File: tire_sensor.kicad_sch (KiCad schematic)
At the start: 30 parts, among them J1 Conn_02x05_Odd_Even, J2 U.FL, U2 DPS368, U3 LIS3DHTR, X1 32MHz, X2 32.768kHz

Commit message: Update JLCPCB part assignments
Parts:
- C7: footprint Capacitor_SMD:C_0402_1005Metric -> PCM_JLCPCB:C_0402; symbol temp_sensor_2-altium-import:root_0_CAP_Nordic Passive DB.DbLib -> PCM_JLCPCB-Capacitors:0402,100pF; Attrition Qty (none) -> 10; Capacitance (none) -> 100pF; Category (none) -> Capacitors,Multilayer Ceramic Capacitors MLCC - SMD/SMT; Class (none) -> Basic Component; LCSC (none) -> C1546; Manufacturer (none) -> FH(Guangdong Fenghua Advanced Tech); Minimum Qty (none) -> 20; Part (none) -> 0402CG101J500NT; Price (none) -> 0.004USD; Process (none) -> SMT; Stock (none) -> 3286274; Temperature Coefficient (none) -> C0G; Tolerance (none) -> ±5%; Voltage Rated (none) -> 50V
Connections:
- net DEC3: now also C7.1
- net GND: now also C7.2
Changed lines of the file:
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@@
 	(wire
 		(pts
-			(xy 207.01 105.41) (xy 210.82 105.41)
-		)
-		(stroke
-			(width 0)
-			(type default)
-		)
-	)
-	(wire
-		(pts
 			(xy 259.08 30.48) (xy 274.32 30.48)
 		)
@@
 	(wire
 		(pts
+			(xy 207.01 105.41) (xy 210.82 105.41)
+		)
+		(stroke
+			(width 0)
+			(type default)
+		)
+	)
+	(wire
+		(pts
 			(xy 90.17 114.3) (xy 115.57 114.3)
 		)
@@
 	)
 	(symbol
-		(lib_id "temp_sensor_2-altium-import:root_0_CAP_Nordic Passive DB.DbLib")
-		(at 210.82 105.41 0)
-		(unit 0)
+		(lib_id "PCM_JLCPCB-Capacitors:0402,100pF")
+		(at 214.63 105.41 90)
+		(unit 1)
 		(exclude_from_sim no)
 		(in_bom yes)
@@
 		(dnp no)
 		(property "Reference" "C7"
-			(at 213.36 103.378 0)
+			(at 212.598 102.87 0)
 			(effects
 				(font
@@
 		)
 		(property "Value" "100pF"
-			(at 213.36 109.982 0)
+			(at 219.202 102.87 0)
 			(effects
 				(font
@@
 			)
 		)
-		(property "Footprint" "Capacitor_SMD:C_0402_1005Metric"
-			(at 210.82 105.41 0)
+		(property "Footprint" "PCM_JLCPCB:C_0402"
+			(at 214.63 107.188 90)
 			(effects
 				(font
@@
 			)
 		)
-		(property "Datasheet" ""
-			(at 210.82 105.41 0)
+		(property "Datasheet" "https://www.lcsc.com/datasheet/lcsc_datasheet_2304140030_FH--Guangdong-Fenghua-Advanced-Tech-0402CG101J500NT_C1546.pdf"
+			(at 214.63 105.41 0)
 			(effects
 				(font
@@
 			)
 		)
-		(property "Description" "Capacitor, NP0, ±5%"
-			(at 210.82 105.41 0)
+		(property "Description" "50V 100pF C0G ±5% 0402 Multilayer Ceramic Capacitors MLCC - SMD/SMT ROHS"
+			(at 214.63 105.41 0)
 			(effects
 				(font
@@
 		)
 		(property "PART NUMBER" "C0402-100p"
-			(at 210.312 103.378 0)
+			(at 212.598 105.918 0)
 			(effects
 				(font
@@
 		)
 		(property "MANUFACTURER" "*"
-			(at 210.312 103.378 0)
+			(at 212.598 105.918 0)
 			(effects
 				(font
@@
 		)
 		(property "MANUFACTURER PART NUMBER" "*"
-			(at 210.312 103.378 0)
+			(at 212.598 105.918 0)
 			(effects
 				(font
@@
 		)
 		(property "DATASHEET" "*"
-			(at 210.312 103.378 0)
+			(at 212.598 105.918 0)
 			(effects
 				(font
@@
 		)
 		(property "LATESTREVISIONDATE" "2009-05-08"
-			(at 210.312 103.378 0)
+			(at 212.598 105.918 0)
 			(effects
 				(font
@@
 		)
 		(property "PIN COUNT" "2"
-			(at 210.312 103.378 0)
+			(at 212.598 105.918 0)
 			(effects
 				(font
@@
 		)
 		(property "PUBLISHER" "Nordic Semiconductor"
-			(at 210.312 103.378 0)
+			(at 212.598 105.918 0)
 			(effects
 				(font
@@
 		)
 		(property "PUBLISHED" "2009-05-08"
-			(at 210.312 103.378 0)
+			(at 212.598 105.918 0)
 			(effects
 				(font
@@
 		)
 		(property "ALTIUM_VALUE" "100pF"
-			(at 210.312 103.378 0)
+			(at 212.598 105.918 0)
 			(effects
 				(font
@@
 		)
 		(property "NOTE" "50V"
-			(at 210.312 103.378 0)
+			(at 212.598 105.918 0)
 			(effects
 				(font
@@
 		)
 		(property "SUPPLIER" "*"
-			(at 210.312 103.378 0)
+			(at 212.598 105.918 0)
 			(effects
 				(font
@@
 		)
 		(property "SUPPLIER PART NUMBER" "*"
-			(at 210.312 103.378 0)
+			(at 212.598 105.918 0)
 			(effects
 				(font
@@
 		)
 		(property "2ND SOURCE SUPPLIER" "*"
-			(at 210.312 103.378 0)
+			(at 212.598 105.918 0)
 			(effects
 				(font
@@
 		)
 		(property "2ND SOURCE PART NUMBER" "*"
-			(at 210.312 103.378 0)
+			(at 212.598 105.918 0)
 			(effects
 				(font
@@
 		)
 		(property "ARTIKKELNR NOCA" "20029135"
-			(at 210.312 103.378 0)
+			(at 212.598 105.918 0)
 			(effects
 				(font
@@
 		)
 		(property "FOOTPRINT DOC" "0402"
-			(at 210.312 103.378 0)
+			(at 212.598 105.918 0)
 			(effects
 				(font
@@
 		)
 		(property "ARTIKKELNR SIMPRO" "N.A."
-			(at 210.312 103.378 0)
+			(at 212.598 105.918 0)
 			(effects
 				(font
@@
 			)
 		)
+		(property "LCSC" "C1546"
+			(at 214.63 105.41 0)
+			(effects
+				(font
+					(size 1.27 1.27)
+				)
+				(hide yes)
+			)
+		)
+		(property "Stock" "3286274"
+			(at 214.63 105.41 0)
+			(effects
+				(font
+					(size 1.27 1.27)
+				)
+				(hide yes)
+			)
+		)
+		(property "Price" "0.004USD"
+			(at 214.63 105.41 0)
+			(effects
+				(font
+					(size 1.27 1.27)
+				)
+				(hide yes)
+			)
+		)
+		(property "Process" "SMT"
+			(at 214.63 105.41 0)
+			(effects
+				(font
+					(size 1.27 1.27)
+				)
+				(hide yes)
+			)
+		)
+		(property "Minimum Qty" "20"
+			(at 214.63 105.41 0)
+			(effects
+				(font
+					(size 1.27 1.27)
+				)
+				(hide yes)
+			)
+		)
+		(property "Attrition Qty" "10"
+			(at 214.63 105.41 0)
+			(effects
+				(font
+					(size 1.27 1.27)
+				)
+				(hide yes)
+			)
+		)
+		(property "Class" "Basic Component"
+			(at 214.63 105.41 0)
+			(effects
+				(font
+					(size 1.27 1.27)
+				)
+				(hide yes)
+			)
+		)
+		(property "Category" "Capacitors,Multilayer Ceramic Capacitors MLCC - SMD/SMT"
+			(at 214.63 105.41 0)
+			(effects
+				(font
+					(size 1.27 1.27)
+				)
+				(hide yes)
+			)
+		)
+		(property "Manufacturer" "FH(Guangdong Fenghua Advanced Tech)"
+			(at 214.63 105.41 0)
+			(effects
+				(font
+					(size 1.27 1.27)
+				)
+				(hide yes)
+			)
+		)
+		(property "Part" "0402CG101J500NT"
+			(at 214.63 105.41 0)
+			(effects
+				(font
+					(size 1.27 1.27)
+				)
+				(hide yes)
+			)
+		)
+		(property "Voltage Rated" "50V"
+			(at 216.6762 103.378 0)
+			(effects
+				(font
+					(size 0.8 0.8)
+				)
+				(justify left)
+			)
+		)
+		(property "Tolerance" "±5%"
+			(at 214.63 105.41 0)
+			(effects
+				(font
+					(size 1.27 1.27)
+				)
+				(hide yes)
+			)
+		)
+		(property "Capacitance" "100pF"
+			(at 214.63 105.41 0)
+			(effects
+				(font
+					(size 1.27 1.27)
+				)
+				(hide yes)
+			)
+		)
+		(property "Temperature Coefficient" "C0G"
+			(at 214.63 105.41 0)
+			(effects
+				(font
+					(size 1.27 1.27)
+				)
+				(hide yes)
+			)
+		)
 		(pin "2"
 		)
@@
 				(path "/12e84b5e-0aa3-44f3-a9b4-3da4f6300b1b"
 					(reference "C7")
-					(unit 0)
+					(unit 1)
 				)
 			)

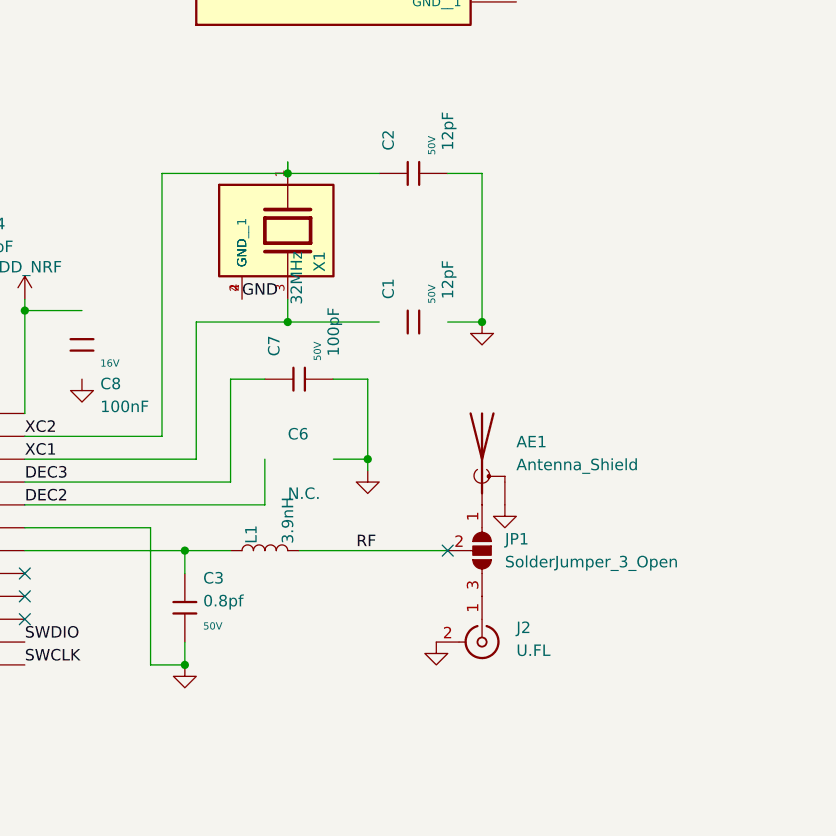
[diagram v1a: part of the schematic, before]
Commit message: JCLPCB updated Crystal per stock, other fixes
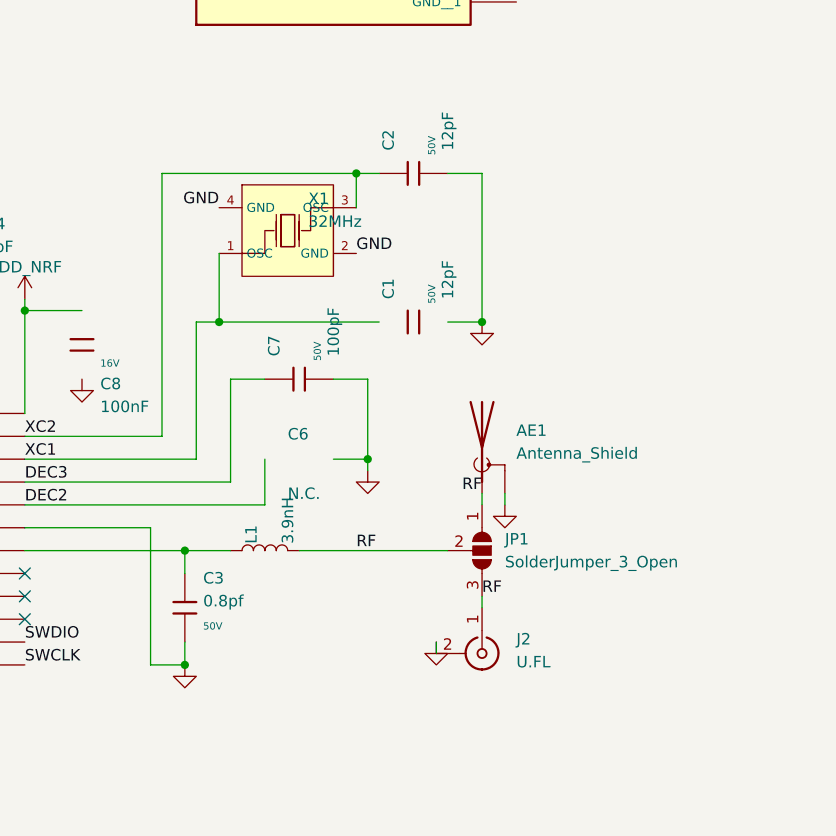
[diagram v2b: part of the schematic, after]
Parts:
- X1: footprint footprints:XTAL_FA-128_32.0000MF20X-K3 -> PCM_JLCPCB:OSC-SMD_4P-L3.2-W2.5-BL_SIT8008BI; symbol FA-128_32.0000MF20X-K3:FA-128_32.0000MF20X-K3 -> PCM_JLCPCB-Extended:Crystal, 40MHz, 15pF; LCSC (none) -> C9010; PartID (none) -> X322540MPB4SI
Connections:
- net RF: now also AE1.1 (A), J2.1 (In), JP1.1 (A), JP1.3 (B)
- net XC1: now also X1.1 (OSC); no longer X1.3
- net XC2: now also X1.3 (OSC); no longer X1.1
- no-connect marks 30 -> 29
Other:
- moved on the sheet: AE1, J2

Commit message: No uFL, LEDs, button
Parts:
- removed J2: U.FL, PCM_JLCPCB:IPEX-SMD_BWIPX-1-001E, symbol PCM_JLCPCB-Extended:RF, Connector, U.FL
- removed JP1: SolderJumper_3_Open, Jumper:SolderJumper-3_P1.3mm_Open_RoundedPad1.0x1.5mm, symbol Jumper:SolderJumper_3_Open
- added D1, D2, D3, D4, D5: LED, LED_SMD:LED_0603_1608Metric, symbol Device:LED
- added R1, R2, R3, R4, R5: 1kΩ, PCM_JLCPCB:R_0402, symbol PCM_JLCPCB-Resistors:0402,1kΩ
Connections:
- net VDD_NRF: now also D1.2 (A), D2.2 (A), D3.2 (A), D4.2 (A), D5.2 (A)
- net LED0: now reaches U1.40 (P0.28/AIN4)
- net LED0: now also R1.2
- net LED1: now reaches U1.41 (P0.29/AIN5)
- net LED1: now also R2.2
- net LED2: now reaches U1.42 (P0.30/AIN6)
- net LED2: now also R3.2
- net LED3: now reaches U1.43 (P0.31/AIN7)
- net LED3: now also R4.2
- net LED4: now reaches U1.44 (N.C.)
- net LED4: now also R5.2
- new net: D3.1 (K), R3.1
- new net: D1.1 (K), R1.1
- new net: D5.1 (K), R5.1
- new net: D2.1 (K), R2.1
- new net: D4.1 (K), R4.1
- no-connect marks 29 -> 24
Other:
- moved on the sheet: J1

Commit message: Schematic saved
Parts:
- added R6: 10kΩ, PCM_JLCPCB:R_0402, symbol PCM_JLCPCB-Resistors:0402,10kΩ
- added S1: Tactile Button, 160gf, PCM_JLCPCB:SW_TS-1088-AR02016, symbol PCM_JLCPCB-Connectors_Buttons:Tactile Button, 160gf, 12V, 50mA, 4.0mm
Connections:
- net GND: now also S1.2 (B)
- net VDD_NRF: now also R6.1
- net BTN: now reaches U1.12 (P0.10)
- net BTN: now also R6.2, S1.1 (A)
- no-connect marks 24 -> 23
